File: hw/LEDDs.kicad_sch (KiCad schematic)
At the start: 3 parts

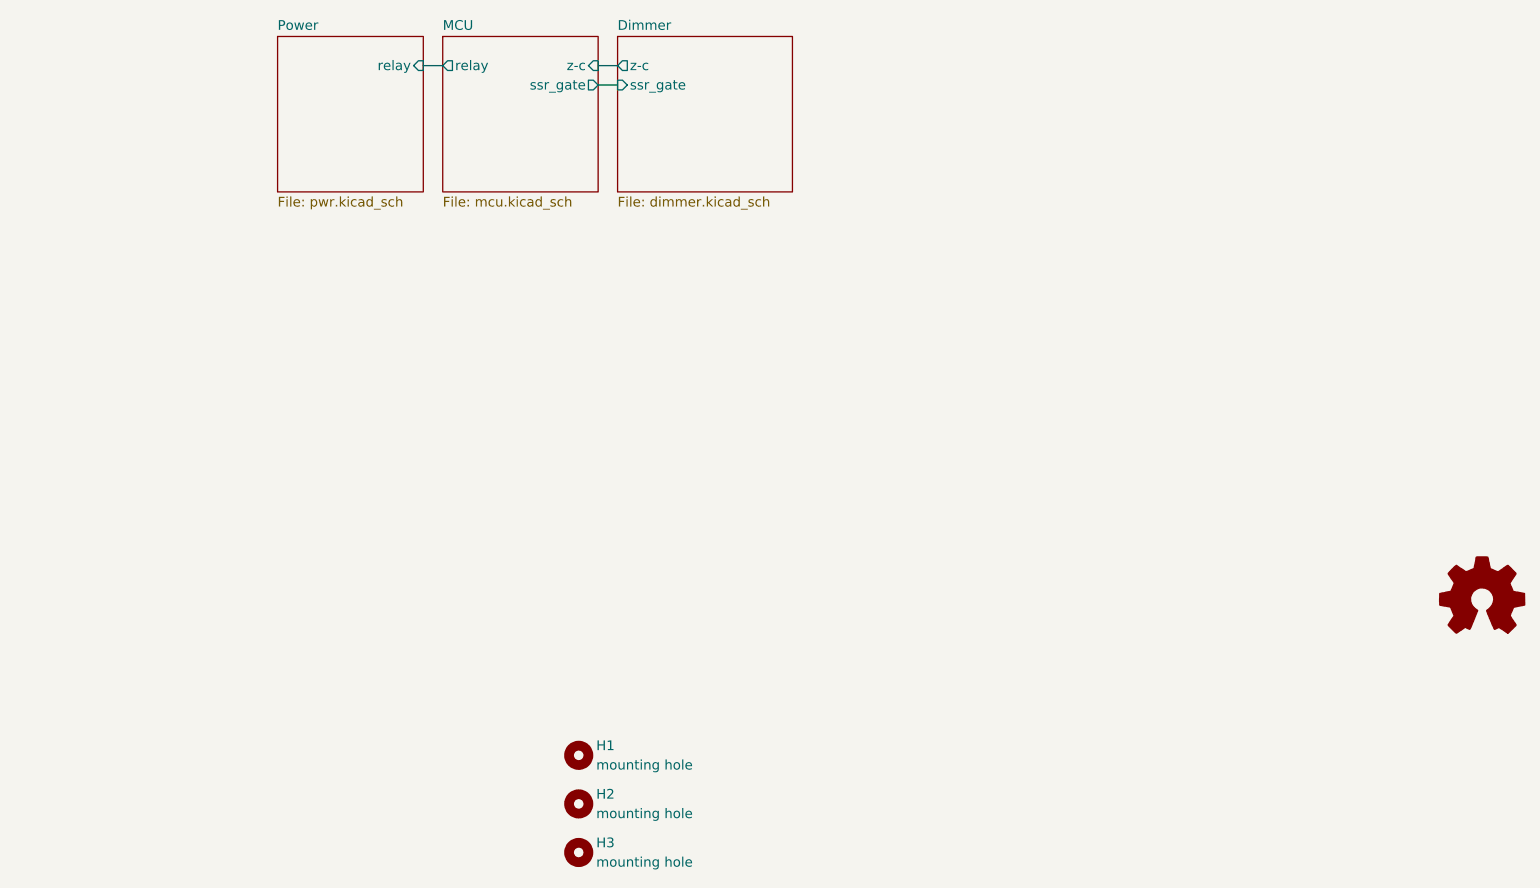
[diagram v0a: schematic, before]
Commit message: V2.0 (#2)
* **Hardware & Mechanical Design**
  * Updated design files and exports.
  * Split chassis and top plate into variants.
  * Changed enclosure folder structure.
  * Hid alignment/dimension layers; removed duplicate models.
  * Added mechanical parts and notes to schematics.

* **Firmware**
  * Updated firmware and added new versions.
  * Introduced firmware variants and consolidated them into packages.
  * Added common.yaml.
  * Moved effects out of packages.

* **Project Structure & Tooling**
  * Added BOM exports and fixed script permissions.
  * Updated and cleaned export folders.
  * Added ESPHome auto-generated `.gitignore`.
  * Fixed included libraries.
  * Miscellaneous corrections, reviews, merges, and cleanup commits.

* **Documentation & README**
  * Multiple revisions for clarity, formatting, structure, and consistency.
  * Added safety warnings for mains voltage operation.
  * Updated table of contents, badges, links, images, and repository structure sections.
  * Added roadmap, split release and change logs, reformatted release log.
  * Added links to schematic, PCB, BOMs, and iBOM.
  * Added additional documentation files.

* **Images, Photos & Media**
  * Updated, renamed, resized, and reformatted images.
  * Improved README image layout (width adjustments, centering, reduced size).
  * Added photos and screenshots across README and sub-readmes.
  * Added animations and animation exports; removed obsolete images.
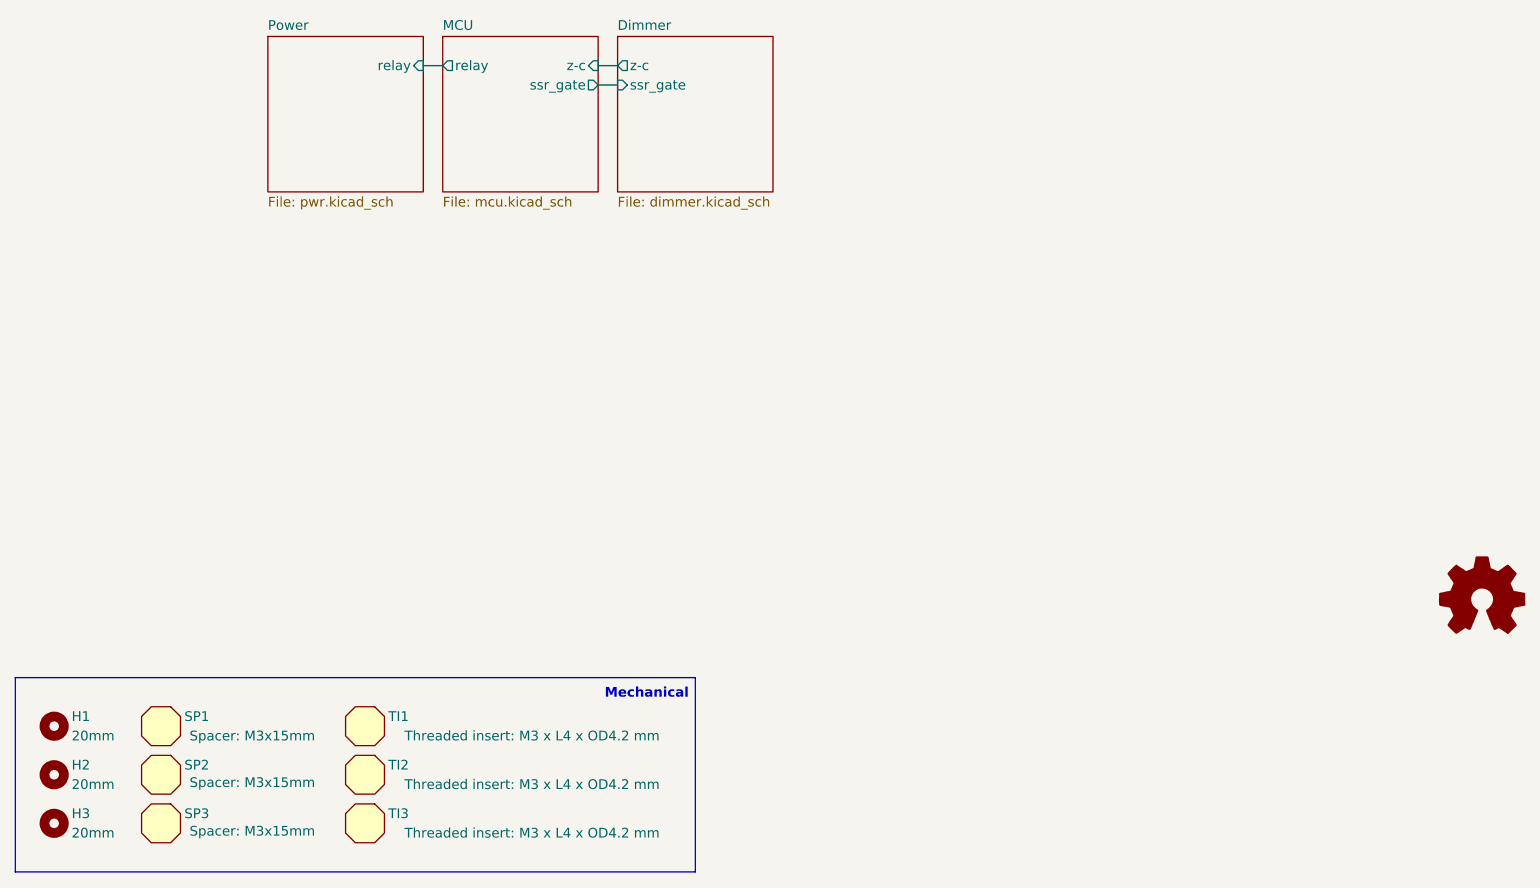
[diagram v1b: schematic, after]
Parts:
- added SP1, SP2, SP3: 15mm, symbol Mechanical:Mechanical_Shape
- added TI1, TI2, TI3: 4x4.2 mm, symbol Mechanical:Mechanical_Shape
- H1, H2, H3: value mounting hole -> 20mm; now in the parts list
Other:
- moved on the sheet: H1, H2, H3
